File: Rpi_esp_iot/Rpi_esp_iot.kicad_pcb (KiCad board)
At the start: 2 copper layers, 114 parts, among them J3 USB_C_Receptacle_USB2.0_16P, Q1 MMDT3904, U1 ST4SI2M0020TPIFW, U2 RASPBERRYPI-ZERO, U3 SHT30-DIS, U4 MLX90614ESF-AAA-000-TU-ND, U5 SIM7070G, U6 ESP32-C6-MINI-1, U7 NXB0104PWJ, U9 MCP6001x-LT

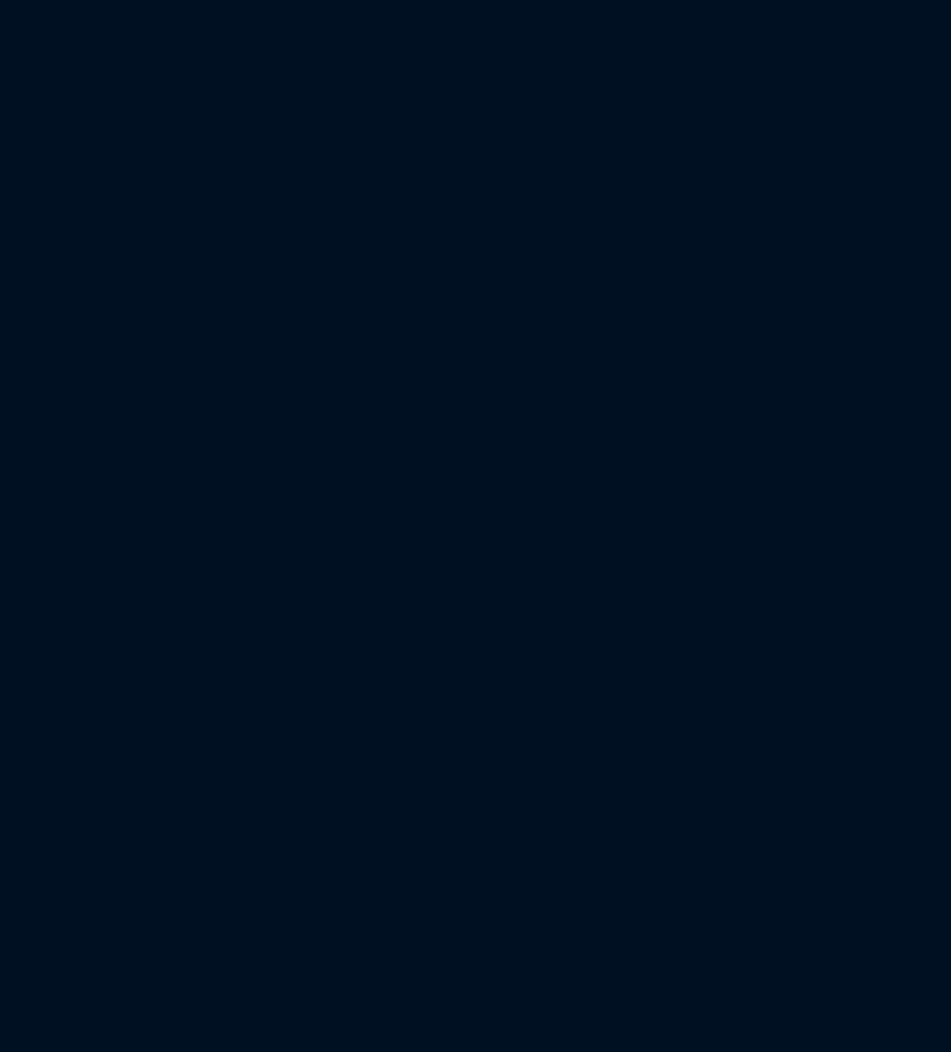
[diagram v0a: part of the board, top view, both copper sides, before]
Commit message: Solar Charge Controller added and layout is improved
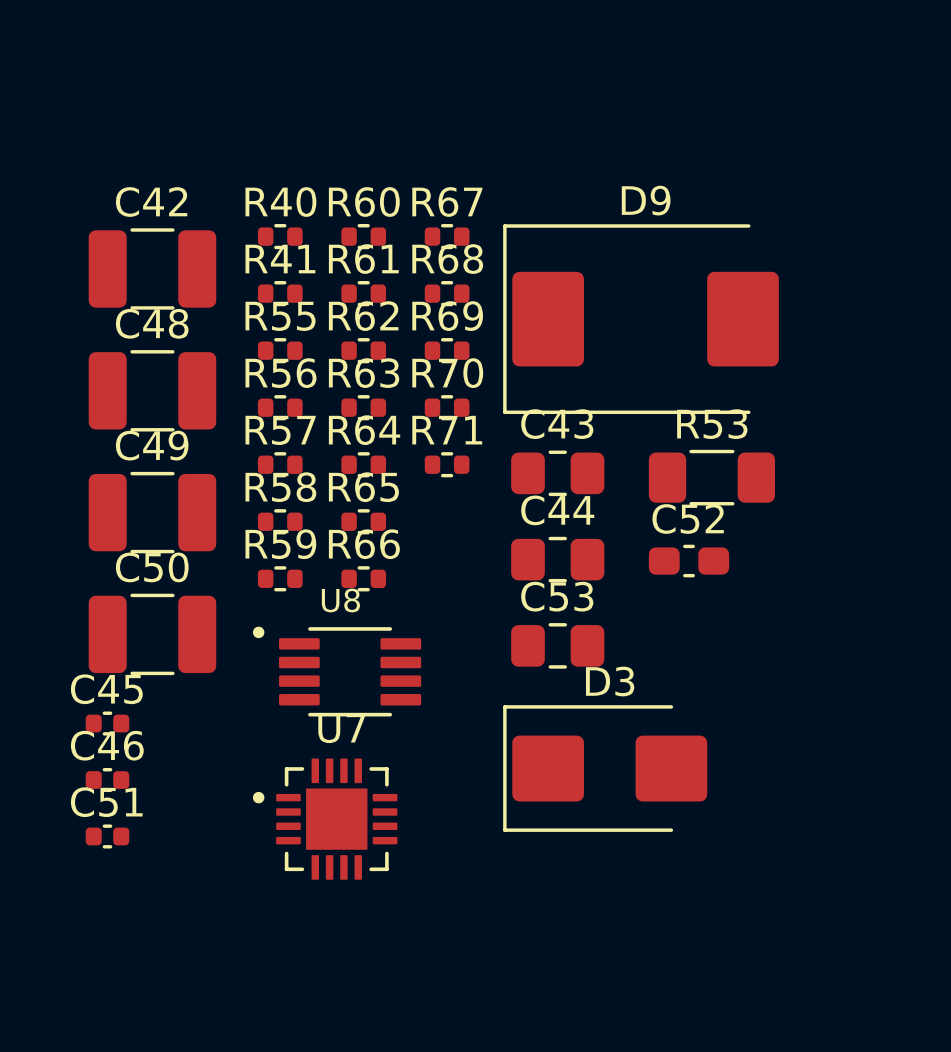
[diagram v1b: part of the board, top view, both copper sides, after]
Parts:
- added C42: 2.2uF, Capacitor_SMD:C_1210_3225Metric_Pad1.33x2.70mm_HandSolder, F.Cu at (71.7, 108.6)
- added C43: 1uF, Capacitor_SMD:C_0805_2012Metric_Pad1.18x1.45mm_HandSolder, F.Cu at (85.9, 115.8)
- added C44: 1uF, Capacitor_SMD:C_0805_2012Metric_Pad1.18x1.45mm_HandSolder, F.Cu at (85.9, 118.8)
- added C45: 0.1uF, Capacitor_SMD:C_0402_1005Metric, F.Cu at (70.2, 124.5)
- added C46: 100pF, Capacitor_SMD:C_0402_1005Metric, F.Cu at (70.2, 126.5)
- added C48: 10uF, Capacitor_SMD:C_1210_3225Metric_Pad1.33x2.70mm_HandSolder, F.Cu at (71.7, 112.9)
- added C49: 10uF, Capacitor_SMD:C_1210_3225Metric_Pad1.33x2.70mm_HandSolder, F.Cu at (71.7, 117.1)
- added C50: 4.7uF, Capacitor_SMD:C_1210_3225Metric_Pad1.33x2.70mm_HandSolder, F.Cu at (71.7, 121.4)
- added C51: 0.1uF, Capacitor_SMD:C_0402_1005Metric, F.Cu at (70.2, 128.4)
- added C52: 22pF, Capacitor_SMD:C_0603_1608Metric_Pad1.08x0.95mm_HandSolder, F.Cu at (90.5, 118.8)
- added C53: 1uF, Capacitor_SMD:C_0805_2012Metric_Pad1.18x1.45mm_HandSolder, F.Cu at (85.9, 121.8)
- added D3: PDS1040, Diode_SMD:D_SMB, F.Cu at (87.7, 126.1)
- added D9: BAT54C, Diode_SMD:D_SMC, F.Cu at (89.0, 110.4)
- added R40: 0R, Resistor_SMD:R_0402_1005Metric, F.Cu at (76.2, 107.5)
- added R41: 0R, Resistor_SMD:R_0402_1005Metric, F.Cu at (76.2, 109.5)
- added R53: 10R, Resistor_SMD:R_1206_3216Metric_Pad1.30x1.75mm_HandSolder, F.Cu at (91.3, 115.9)
- added R55: 0R, Resistor_SMD:R_0402_1005Metric, F.Cu at (76.2, 111.5)
- added R56: 0R, Resistor_SMD:R_0402_1005Metric, F.Cu at (76.2, 113.5)
- added R57: 10K, Resistor_SMD:R_0402_1005Metric, F.Cu at (76.2, 115.5)
- added R58: 10K, Resistor_SMD:R_0402_1005Metric, F.Cu at (76.2, 117.5)
- added R59: 200K, Resistor_SMD:R_0402_1005Metric, F.Cu at (76.2, 119.5)
- added R60: 5.23K, Resistor_SMD:R_0402_1005Metric, F.Cu at (79.1, 107.5)
- added R61: 30.1K, Resistor_SMD:R_0402_1005Metric, F.Cu at (79.1, 109.5)
- added R62: 499K, Resistor_SMD:R_0402_1005Metric, F.Cu at (79.1, 111.5)
- added R63: 36K, Resistor_SMD:R_0402_1005Metric, F.Cu at (79.1, 113.5)
- added R64: 10K, Resistor_SMD:R_0402_1005Metric, F.Cu at (79.1, 115.5)
- added R65: 10K, Resistor_SMD:R_0402_1005Metric, F.Cu at (79.1, 117.5)
- added R66: 20mR, Resistor_SMD:R_0402_1005Metric, F.Cu at (79.1, 119.5)
- added R67: 499K, Resistor_SMD:R_0402_1005Metric, F.Cu at (82.0, 107.5)
- added R68: 100K, Resistor_SMD:R_0402_1005Metric, F.Cu at (82.0, 109.5)
- added R69: 5.23K, Resistor_SMD:R_0402_1005Metric, F.Cu at (82.0, 111.5)
- added R70: 10K, Resistor_SMD:R_0402_1005Metric, F.Cu at (82.0, 113.5)
- added R71: 10K, Resistor_SMD:R_0402_1005Metric, F.Cu at (82.0, 115.5)
- added U7: BQ24650RVAT, BQ24650RVAT:QFN50P350X350X100-17N, F.Cu at (78.2, 127.8)
- added U8: PCA9306DCTR, PCA9306DCTR:SOP65P400X130-8N, F.Cu at (78.6, 122.7)
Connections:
- net Net-(C41-Pad2) renamed ESIM_DATA
- C3 pad 1: +Vsys -> +Vbat
- C4 pad 1: +Vsys -> +Vbat
- C7 pad 1: +Vsys -> +Vbat
- C8 pad 1: +Vsys -> +Vbat
- R13 pad 1: +5V_SEN -> +5V_RPi
- R13 pad 2: RPI_SDA -> SNS_I2C_SDA
- R14 pad 1: +5V_SEN -> +5V_RPi
- R14 pad 2: RPI_SCL -> SNS_I2C_SCL
- R4 pad 1: +Vsys -> +Vbat
- R8 pad 1: +Vsys -> +Vbat
- U2 pad 29: unconnected-(U2-GPIO5-Pad29) -> SHT_ALT_Rpi
- U3 pad 1: RPI_SDA -> SNS_I2C_SDA
- U3 pad 4: RPI_SCL -> SNS_I2C_SCL
- U4 pad 1: RPI_SCL -> SNS_I2C_SCL
- U4 pad 2: RPI_SDA -> SNS_I2C_SDA
- U5 pad 24: unconnected-(U5-USB_VBUS-Pad24) -> Net-(U5-USB_VBUS)
- U5 pad 27: unconnected-(U5-USB_DP-Pad27) -> Net-(U5-USB_DP)
- U5 pad 28: unconnected-(U5-USB_DM-Pad28) -> Net-(U5-USB_DM)
- U6 pad 24: Net-(U6-IO18) -> BATTERY
- VR2 pad 1: +Vsys -> +Vbat
- VR3 pad 1: +Vsys -> +Vbat

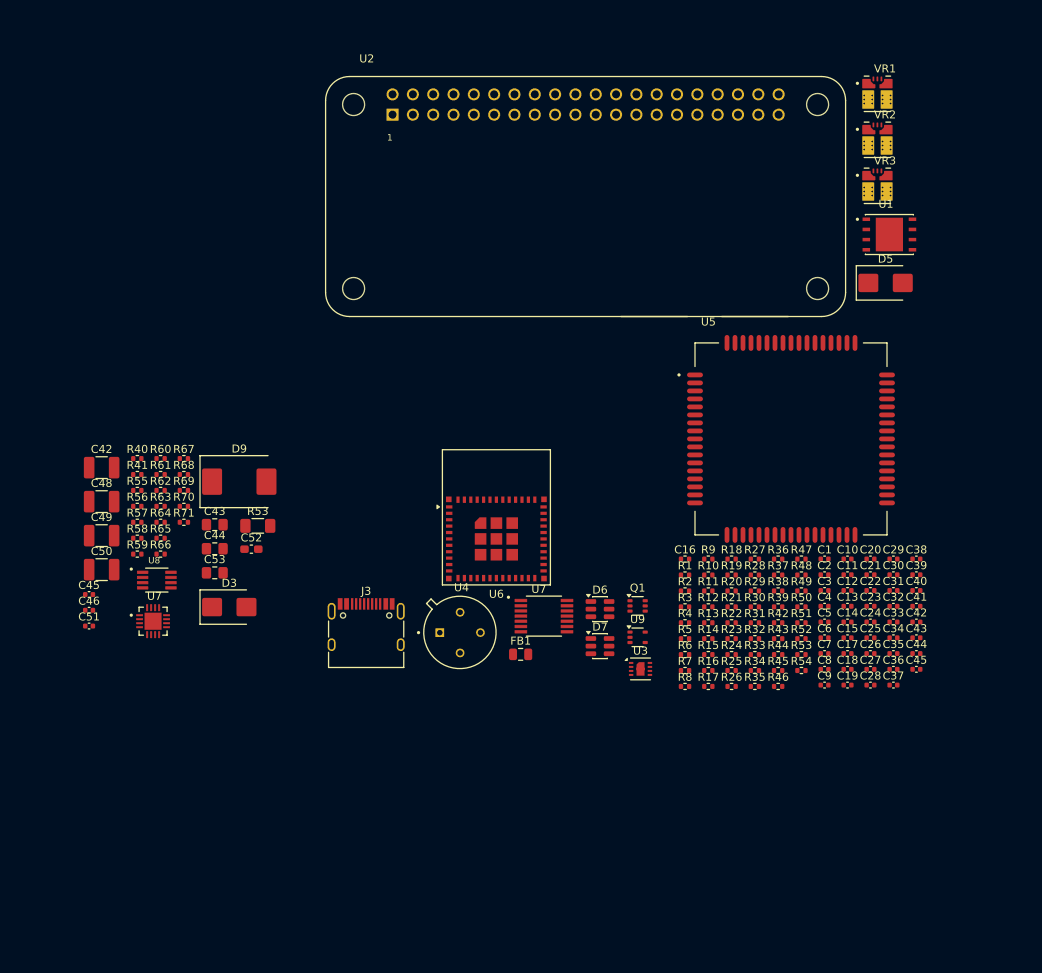
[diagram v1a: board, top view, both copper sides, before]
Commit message: Sourcing Complete + Added all Components to PCB + Resolved errors
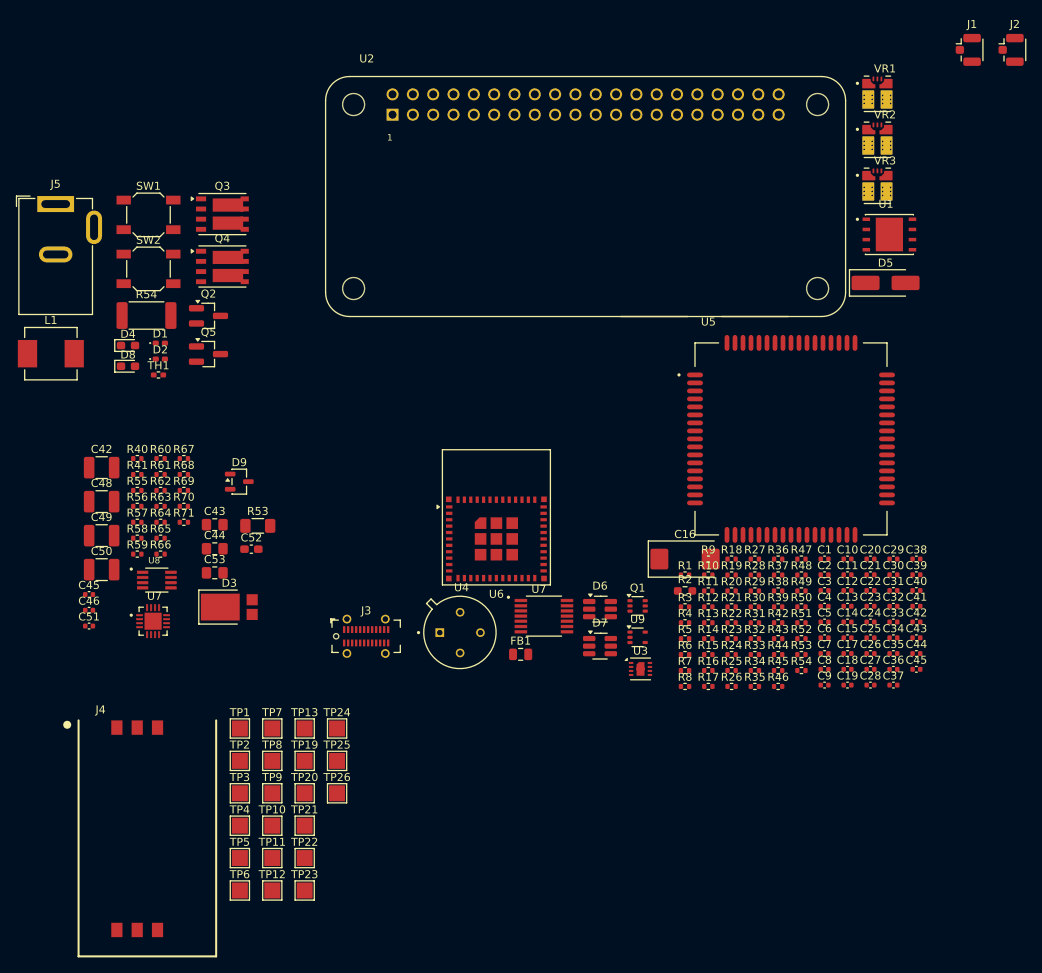
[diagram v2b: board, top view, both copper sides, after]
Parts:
- added D1: XL-1005SURC, LED_SMD:LED_0402_1005Metric_Pad0.77x0.64mm_HandSolder, F.Cu at (79.1, 93.1)
- added D2: XL-1005UGC, LED_SMD:LED_0402_1005Metric_Pad0.77x0.64mm_HandSolder, F.Cu at (79.1, 95.1)
- added D4: LTST-C190GKT, LED_SMD:LED_0603_1608Metric_Pad1.05x0.95mm_HandSolder, F.Cu at (75.0, 93.4)
- added D8: LTST-C190GKT, LED_SMD:LED_0603_1608Metric_Pad1.05x0.95mm_HandSolder, F.Cu at (75.0, 96.0)
- added J1: Conn_01x03, Connector_Coaxial:U.FL_Hirose_U.FL-R-SMT-1_Vertical, F.Cu at (180.1, 56.4)
- added J2: Conn_01x03, Connector_Coaxial:U.FL_Hirose_U.FL-R-SMT-1_Vertical, F.Cu at (185.4, 56.4)
- added J4: 7111S2015X02LF, 7111S2015X02LF:FCI_7111S2015X02LF, F.Cu at (76.2, 153.8)
- added J5: Barrel_Jack_MountingPin, Connector_BarrelJack:BarrelJack_GCT_DCJ200-10-A_Horizontal, F.Cu at (66.0, 75.7)
- added L1: 10uH, Inductor_SMD:L_Vishay_IHLP-2525, F.Cu at (65.4, 94.4)
- added Q2: NMOS, Package_TO_SOT_SMD:SOT-23_Handsoldering, F.Cu at (85.1, 89.7)
- added Q3: Si7288, Package_SO:PowerPAK_SO-8_Dual, F.Cu at (86.8, 77.0)
- added Q4: Si7288, Package_SO:PowerPAK_SO-8_Dual, F.Cu at (86.8, 83.5)
- added Q5: NMOS, Package_TO_SOT_SMD:SOT-23_Handsoldering, F.Cu at (85.1, 94.5)
- added R54: 2R, Resistor_SMD:R_2512_6332Metric_Pad1.40x3.35mm_HandSolder, F.Cu at (77.3, 89.6)
- added SW1: SW_SPST, Button_Switch_SMD:SW_SPST_SKQG_WithStem, F.Cu at (77.6, 77.0)
- added SW2: SW_SPST, Button_Switch_SMD:SW_SPST_SKQG_WithStem, F.Cu at (77.6, 83.8)
- added TH1: Thermistor_NTC, Resistor_SMD:R_0402_1005Metric_Pad0.72x0.64mm_HandSolder, F.Cu at (78.8, 97.1)
- added TP1: TestPoint, TestPoint:TestPoint_Pad_2.0x2.0mm, F.Cu at (89.0, 141.2)
- added TP10: TestPoint, TestPoint:TestPoint_Pad_2.0x2.0mm, F.Cu at (93.1, 153.4)
- added TP11: TestPoint, TestPoint:TestPoint_Pad_2.0x2.0mm, F.Cu at (93.1, 157.4)
- added TP12: TestPoint, TestPoint:TestPoint_Pad_2.0x2.0mm, F.Cu at (93.1, 161.5)
- added TP13: TestPoint, TestPoint:TestPoint_Pad_2.0x2.0mm, F.Cu at (97.1, 141.2)
- added TP19: TestPoint, TestPoint:TestPoint_Pad_2.0x2.0mm, F.Cu at (97.1, 145.3)
- added TP2: TestPoint, TestPoint:TestPoint_Pad_2.0x2.0mm, F.Cu at (89.0, 145.3)
- added TP20: TestPoint, TestPoint:TestPoint_Pad_2.0x2.0mm, F.Cu at (97.1, 149.3)
- added TP21: TestPoint, TestPoint:TestPoint_Pad_2.0x2.0mm, F.Cu at (97.1, 153.4)
- added TP22: TestPoint, TestPoint:TestPoint_Pad_2.0x2.0mm, F.Cu at (97.1, 157.4)
- added TP23: TestPoint, TestPoint:TestPoint_Pad_2.0x2.0mm, F.Cu at (97.1, 161.5)
- added TP24: TestPoint, TestPoint:TestPoint_Pad_2.0x2.0mm, F.Cu at (101.2, 141.2)
- added TP25: TestPoint, TestPoint:TestPoint_Pad_2.0x2.0mm, F.Cu at (101.2, 145.3)
- added TP26: TestPoint, TestPoint:TestPoint_Pad_2.0x2.0mm, F.Cu at (101.2, 149.3)
- added TP3: TestPoint, TestPoint:TestPoint_Pad_2.0x2.0mm, F.Cu at (89.0, 149.3)
- added TP4: TestPoint, TestPoint:TestPoint_Pad_2.0x2.0mm, F.Cu at (89.0, 153.4)
- added TP5: TestPoint, TestPoint:TestPoint_Pad_2.0x2.0mm, F.Cu at (89.0, 157.4)
- added TP6: TestPoint, TestPoint:TestPoint_Pad_2.0x2.0mm, F.Cu at (89.0, 161.5)
- added TP7: TestPoint, TestPoint:TestPoint_Pad_2.0x2.0mm, F.Cu at (93.1, 141.2)
- added TP8: TestPoint, TestPoint:TestPoint_Pad_2.0x2.0mm, F.Cu at (93.1, 145.3)
- added TP9: TestPoint, TestPoint:TestPoint_Pad_2.0x2.0mm, F.Cu at (93.1, 149.3)
- C16: value 470Uf -> 470uf; footprint Resistor_SMD:R_0402_1005Metric -> Capacitor_Tantalum_SMD:CP_EIA-7343-15_Kemet-W_HandSolder
- C30, C4, C45, C51, C8: value 0.1uF -> 100nF
- C46: value 100pF -> 1000pF
- D3: footprint Diode_SMD:D_SMB -> Diode_SMD:D_PowerDI-5
- D5: value S2JTR -> SS54; footprint Diode_SMD:D_SMB -> Diode_SMD:D_SMA_Handsoldering
- D6, D7: footprint Package_TO_SOT_SMD:SOT-23-6 -> Package_TO_SOT_SMD:SOT-23-6_Handsoldering
- D9: footprint Diode_SMD:D_SMC -> Package_TO_SOT_SMD:SOT-23-3
- J3: footprint Connector_USB:USB_C_Receptacle_HRO_TYPE-C-31-M-12 -> Connector_USB:USB_C_Receptacle_GCT_USB4115-03-C
- R2: footprint Resistor_SMD:R_0402_1005Metric -> Resistor_SMD:R_0603_1608Metric_Pad0.98x0.95mm_HandSolder
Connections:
- C46 pad 2: +5V_RPi -> Net-(U8-EN)
- R13 pad 1: +5V_RPi -> Net-(U8-EN)
- R14 pad 1: +5V_RPi -> Net-(U8-EN)
- U8 pad 7: +5V_RPi -> Net-(U8-EN)

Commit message: Placement by usama
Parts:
- removed the C42 at (173.6, 127.9)
- removed the C43 at (173.6, 129.9)
- removed the C44 at (173.6, 131.9)
- removed the C45 at (173.6, 133.9)
- removed J4: 7111S2015X02LF, 7111S2015X02LF:FCI_7111S2015X02LF
- removed R52: 0R, Resistor_SMD:R_0402_1005Metric
- removed the R53 at (159.2, 132.0)
- removed the R54 at (77.3, 89.6)
- removed TP1, TP10, TP11, TP12, TP13, TP19, TP2, TP20, TP21, TP22, TP23, TP24, TP25, TP26, TP3, TP4, TP5, TP6, TP7, TP8, TP9: TestPoint, TestPoint:TestPoint_Pad_2.0x2.0mm
- removed the U7 at (127.0, 127.2)
- added H1: MountingHole_Pad, MountingHole:MountingHole_3.2mm_M3_DIN965_Pad, F.Cu at (155.9, 86.2)
- added H2: MountingHole_Pad, MountingHole:MountingHole_3.2mm_M3_DIN965_Pad, F.Cu at (203.9, 75.9)
- added H3: MountingHole_Pad, MountingHole:MountingHole_3.2mm_M3_DIN965_Pad, F.Cu at (94.2, 64.7)
- added H4: MountingHole_Pad, MountingHole:MountingHole_3.2mm_M3_DIN965_Pad, F.Cu at (95.0, 114.8)
- added H5: MountingHole_Pad, MountingHole:MountingHole_3.2mm_M3_DIN965_Pad, F.Cu at (180.3, 112.7)
- added J6: SIM8066-6-1-14-01-A_REVA, Rpi_esp_iot:GCT_SIM8066-6-1-14-01-A_REVA, F.Cu at (98.8, 91.7)
- R42, R43: value 10K -> 5.1K
- R54: value 10K -> 2R; footprint Resistor_SMD:R_0402_1005Metric -> Resistor_SMD:R_2512_6332Metric_Pad1.40x3.35mm_HandSolder
- moved R54 174.8 mm to (30.3, 16.0)
- moved C1 140.1 mm to (54.8, 29.9)
- moved C2 140.1 mm to (54.8, 31.9)
- moved C3 140.1 mm to (54.8, 33.9)
- moved C4 140.1 mm to (54.8, 35.9)
- moved C5 140.1 mm to (54.8, 37.8)
- moved C6 140.1 mm to (54.8, 39.8)
- moved D5 140.1 mm to (62.4, -4.56)
- moved C16 140.1 mm to (37.4, 30.0)
- moved C20 140.1 mm to (60.5, 29.9)
- moved C21 140.1 mm to (60.5, 31.9)
- moved C22 140.1 mm to (60.5, 33.9)
- moved C23 140.1 mm to (60.5, 35.9)
- moved C24 140.1 mm to (60.5, 37.8)
- moved C25 140.1 mm to (60.5, 39.8)
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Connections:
- C41 pad 2: ESIM_DATA -> ESIM_VCC
- D7 pad 4: /ES_DATA_EN -> ESIM_VCC
- D7 pad 6: unconnected-(D7-TVS4-Pad6) -> /ES_DATA_EN
- R19 pad 1: SIM_VCC -> PSIM_VCC
- R54 pad 1: Net-(U7-OE) -> VIN
- R54 pad 2: GND -> Net-(C42-Pad2)
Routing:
- net ESIM_VCC: track 0.00 -> 10.2 mm
- net Net-(U5-SIM_VDD): track 0.00 -> 6.38 mm
- net Net-(U5-SIM_RST): track 0.00 -> 6.16 mm
- net Net-(U5-SIM_DATA): track 0.00 -> 5.89 mm
- net Net-(U5-SIM_CLK): track 0.00 -> 5.67 mm
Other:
- board outline added: 120 x 70 mm

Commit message: Complete Placement + Partial modification in Schematic(Sim+simreset+Power Connection wit diode
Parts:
- removed J5: Barrel_Jack_MountingPin, Connector_BarrelJack:BarrelJack_GCT_DCJ200-10-A_Horizontal
- added D10: SS26, Diode_SMD:D_SMA_Handsoldering, F.Cu at (166.3, 65.5)
- added Q6: MMDT3904, Package_TO_SOT_SMD:SOT-363_SC-70-6, F.Cu at (151.0, 94.3)
- added R52: 20k, Resistor_SMD:R_0402_1005Metric, F.Cu at (94.1, 105.5)
- added R72: 4.7K, Resistor_SMD:R_0402_1005Metric, F.Cu at (146.6, 91.8)
- added R74: 47K, Resistor_SMD:R_0402_1005Metric, F.Cu at (146.6, 96.2)
- added TP14: TestPoint, TestPoint:TestPoint_Pad_2.0x2.0mm, F.Cu at (184.2, 51.3)
- added TP15: TestPoint, TestPoint:TestPoint_Pad_2.0x2.0mm, F.Cu at (192.8, 51.4)
- added TP16: BAT +, TestPoint:TestPoint_Pad_2.0x2.0mm, F.Cu at (201.6, 83.7)
- added TP17: BAT-, TestPoint:TestPoint_Pad_2.0x2.0mm, F.Cu at (201.6, 90.3)
- D5: value SS54 -> SS26
- J3: footprint Connector_USB:USB_C_Receptacle_GCT_USB4115-03-C -> USB4115_03_C:USB4115-03-C_GCT
- Q3, Q4: value Si7288 -> CSD18540Q5B; footprint Package_SO:PowerPAK_SO-8_Dual -> CSD18540Q5B:CSD18540Q5B
- moved L1 246.4 mm to (193.9, 75.5), turned to -90 degrees
- moved C50 236.3 mm to (194.8, 83.7), turned to -90 degrees
- moved SW2 234.8 mm to (172.9, 112.3), turned to 90 degrees
- moved C49 232.7 mm to (190.1, 83.8), turned to 90 degrees
- moved SW1 232.5 mm to (172.5, 101.7), turned to 90 degrees
- moved C42 232.3 mm to (193.0, 60.3)
- moved C51 229.1 mm to (188.3, 79.1), turned to -90 degrees
- moved Q4 226.5 mm to (193.9, 66.5), turned to -90 degrees
- moved C44 225.4 mm to (198.8, 76.5), turned to 90 degrees
- moved C45 225.2 mm to (184.6, 73.5)
- moved D9 223.9 mm to (199.8, 70.7)
- moved R66 223.5 mm to (189.7, 79.1), turned to -90 degrees
- moved R68 221.8 mm to (186.5, 85.5), turned to 90 degrees
- moved R67 221.7 mm to (186.5, 83.2), turned to 90 degrees
- moved D2 221.0 mm to (162.6, 116.4), turned to 90 degrees
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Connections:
- C53 pad 1: Net-(U7-VREF) -> Net-(U7-TERM_EN)
- R60 pad 1: Net-(U7-VREF) -> Net-(U7-TERM_EN)
- U2 pad 11: SIM_PWRKEY -> SIM_PWRKEY_Rpi
- U2 pad 14: unconnected-(U2-GND[4]-Pad14) -> GND
- U5 pad 56: VBAT -> SIM_VCC
- U5 pad 57: VBAT -> SIM_VCC
- U7 pad 17: unconnected-(U7-EPAD-Pad17) -> GND
- U7 pad 6: Net-(U7-VREF) -> Net-(U7-TERM_EN)
- U7 pad 7: unconnected-(U7-TERM_EN-Pad7) -> Net-(U7-TERM_EN)
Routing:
- net Net-(D4-K): track 0.00 -> 24.8 mm, vias 0 -> 2
- net Net-(D8-K): track 0.00 -> 23.2 mm, vias 0 -> 2
- net Net-(D9-K): track 0.00 -> 21.6 mm, vias 0 -> 2
- net +Vbat: track 0.00 -> 17.6 mm, vias 0 -> 10
- net Net-(Q2-D): track 0.00 -> 17.0 mm, vias 0 -> 2
- net VIN: track 0.00 -> 16.6 mm
- net Net-(D9-A): track 0.00 -> 16.5 mm
- net Net-(D3-K): track 0.00 -> 16.3 mm
- net Net-(U7-LODRV): track 0.00 -> 15.6 mm, vias 0 -> 2
- net Net-(U7-HIDRV): track 0.00 -> 11.8 mm
- net Net-(U7-VFB): track 0.00 -> 9.14 mm
- net Net-(U7-PH): track 0.00 -> 7.80 mm
- net BAT_TEMP: track 0.00 -> 6.02 mm
- net Net-(D8-A): track 0.00 -> 5.22 mm
- net Net-(D4-A): track 0.00 -> 4.23 mm
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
